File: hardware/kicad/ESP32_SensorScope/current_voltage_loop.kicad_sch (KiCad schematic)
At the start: 0 parts

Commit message: Adde LCD Part
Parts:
- added D1: D_Schottky, symbol Device:D_Schottky
- added F3: Polyfuse, symbol Device:Polyfuse
- added Q1: PMOS, symbol Simulation_SPICE:PMOS
- added Q2: NMOS, symbol Simulation_SPICE:NMOS
- added R13, R50, R51: R, symbol Device:R
- added U18, U19, U20: OPA333xxDBV, Package_TO_SOT_SMD:SOT-23-5, symbol Amplifier_Operational:OPA333xxDBV
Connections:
- new net: D1.1 (K), F3.1, Q2.1 (D)
- new net: Q2.2 (G), R13.2
- new net: Q2.3 (S), R50.2, U20.4 (-)
- new net: R13.1, U20.1
- new net: D1.2 (A), Q1.3 (S)
- new net Vref: U20.3 (+)

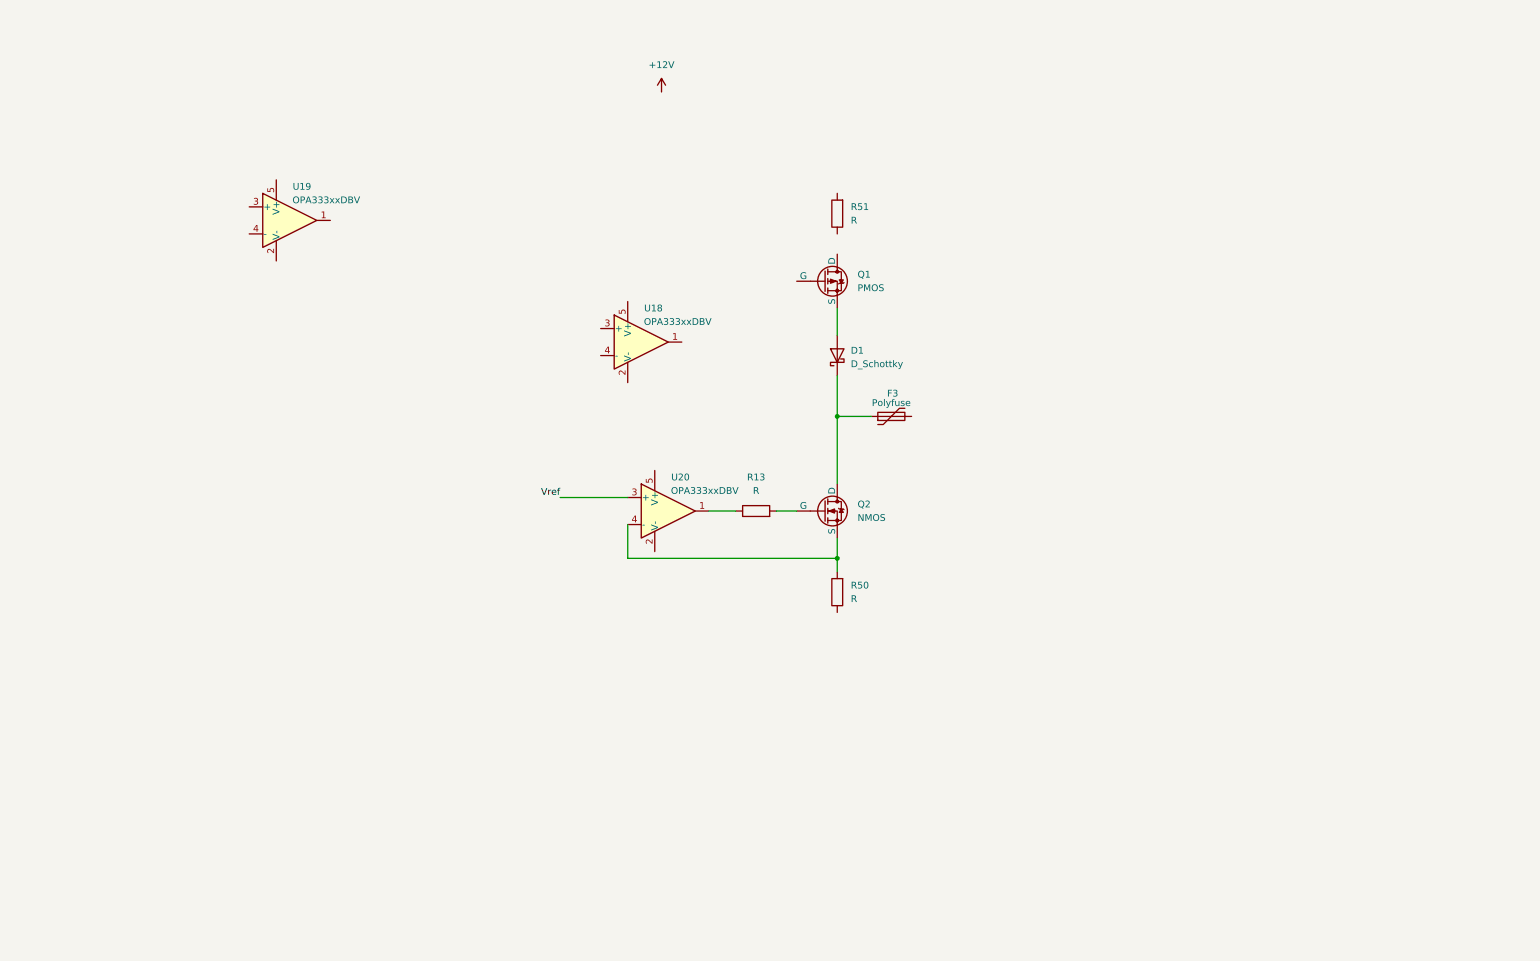
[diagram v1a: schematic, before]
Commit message: updated 4-20mA interface
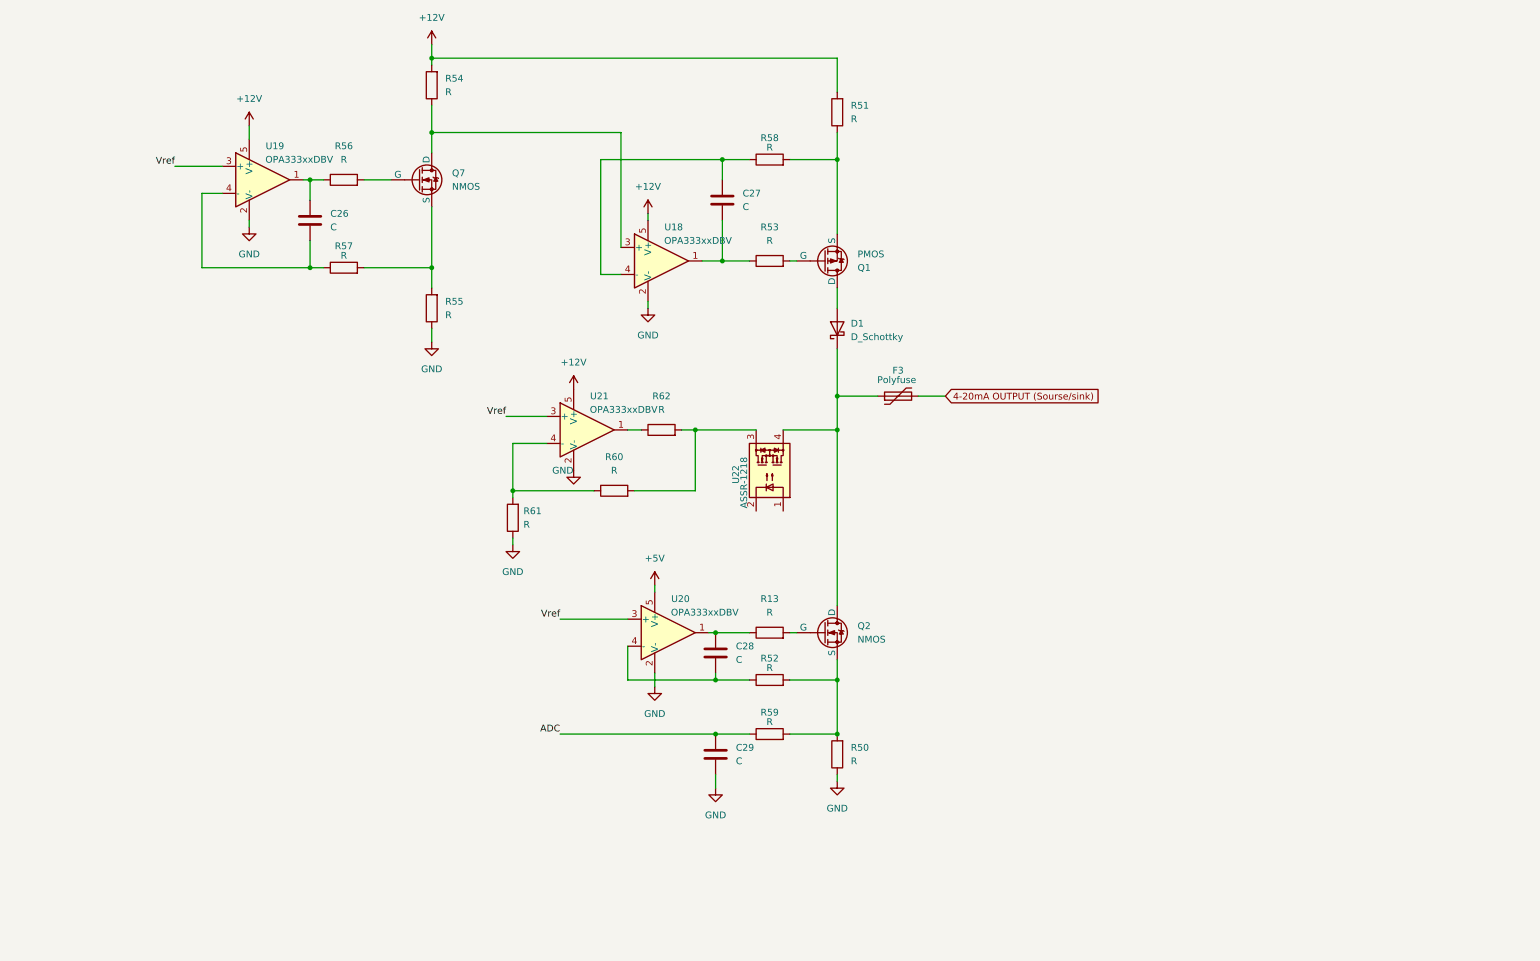
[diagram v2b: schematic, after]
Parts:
- added C26, C27, C28, C29: C, symbol Device:C
- added Q7: NMOS, symbol Simulation_SPICE:NMOS
- added R52, R53, R54, R55, R56, R57, R58, R59, R60, R61, R62: R, symbol Device:R
- added U21: OPA333xxDBV, Package_TO_SOT_SMD:SOT-23-5, symbol Amplifier_Operational:OPA333xxDBV
- added U22: ASSR-1218, Package_SO:SO-4_4.4x4.3mm_P2.54mm, symbol Relay_SolidState:ASSR-1218
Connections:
- net +12V: now also R51.2, U18.5 (V+), U19.5 (V+), R54.2, U21.5 (V+)
- net Vref: now also U19.3 (+), U21.3 (+)
- net at D1.1 (K), F3.1, Q2.1 (D): now also U22.4
- net at Q2.3 (S), R50.2: now also R52.2, R59.2; no longer U20.4 (-)
- net at R51.1: now also Q1.3 (S), R58.2
- net GND: now reaches R50.1
- net GND: now also U18.2 (V-), U19.2 (V-), U20.2 (V-), C29.2, R55.1, R61.1, U21.2 (V-)
- net at U19.1: now also C26.1, R56.1
- net at U19.4 (-): now also C26.2, R57.1
- net at R13.1, U20.1: now also C28.1
- net 4-20mA OUTPUT (Sourse/sink): now reaches F3.2
- net at D1.2 (A): now also Q1.1 (D); no longer Q1.3 (S)
- net +5V: now reaches U20.5 (V+)
- net at U18.1: now also C27.2, R53.1
- net at U18.3 (+): now also Q7.1 (D), R54.1
- net at U18.4 (-): now also C27.1, R58.1
- net at Q1.2 (G): now also R53.2
- new net: R60.2, R62.2, U22.3
- new net: C28.2, R52.1, U20.4 (-)
- new net: Q7.3 (S), R55.2, R57.2
- new net: R62.1, U21.1
- new net: R60.1, R61.2, U21.4 (-)
- new net: Q7.2 (G), R56.2
- new net ADC: C29.1, R59.1
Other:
- moved on the sheet: F3, Q1, Q2, R13, R50, R51, U18, U19, U20

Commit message: something probobly
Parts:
- added D15, D16: 15V, symbol Device:D_Zener
- added D17: D_TVS, symbol Device:D_TVS
- added D2: D_Schottky, symbol Device:D_Schottky
- added Q8: NPN, symbol Simulation_SPICE:NPN
- added Q9: PNP, symbol Simulation_SPICE:PNP
- added R63, R64, R65, R9: 10K, symbol Device:R
- added R66, R8: R, symbol Device:R
- R13, R53: value R -> 100
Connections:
- net +12V: now also D2.1 (K), R66.2
- net +5V: now also Q9.3 (E), R63.1
- net GND: now also D17.1 (A1), Q8.3 (E), R65.2, R8.1
- net at D1.1 (K), F3.1, Q2.1 (D)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: now also D16.1 (K), D17.2 (A2)
- net at Q2.2 (G), R13.2: now also D16.2 (A)
- net at Q1.3 (S), R51.1, R58.2: now also D15.1 (K)
- net at C27.2, R53.1, U18.1: now also R66.1, R9.2
- net at Q1.2 (G), R53.2: now also D15.2 (A)
- net at R62.1, U21.1: now also D2.2 (A)
- net at C28.1, R13.1, U20.1: now also R64.2, R8.2
- net ADC renamed mA_ADC
- new net: Q8.2 (B), R9.1
- new net: Q9.2 (B), R64.1
- new net Highside_Open: Q8.1 (C), R63.2
- new net Lowside_open: Q9.1 (C), R65.1
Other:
- note added: "OP-amps with shutdown OPA991 40V rail to rail, 75mA output, 125uV offset, 4.5MHz OPA990 40V rail to rail, 80mA output, 300uV offset, 1.1MHz TLV237x 16V 2000uV"
- moved on the sheet: C26, C27, C28, C29, F3, Q1, Q2, Q7, R13, R50, R51, R52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

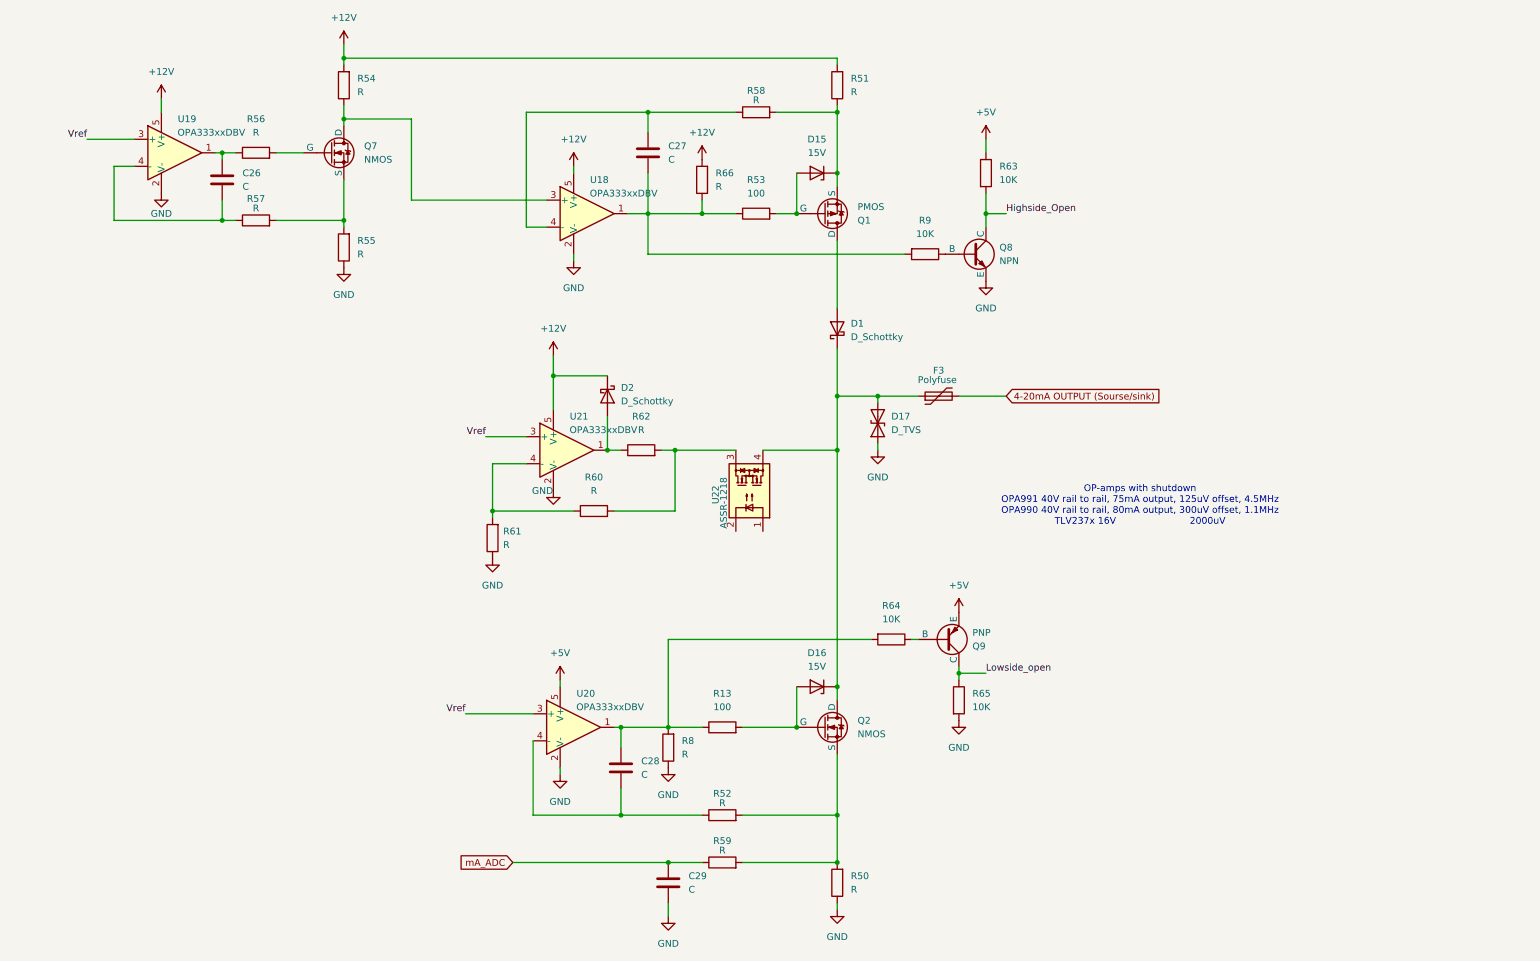
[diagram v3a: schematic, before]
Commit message: som updates on the schematics
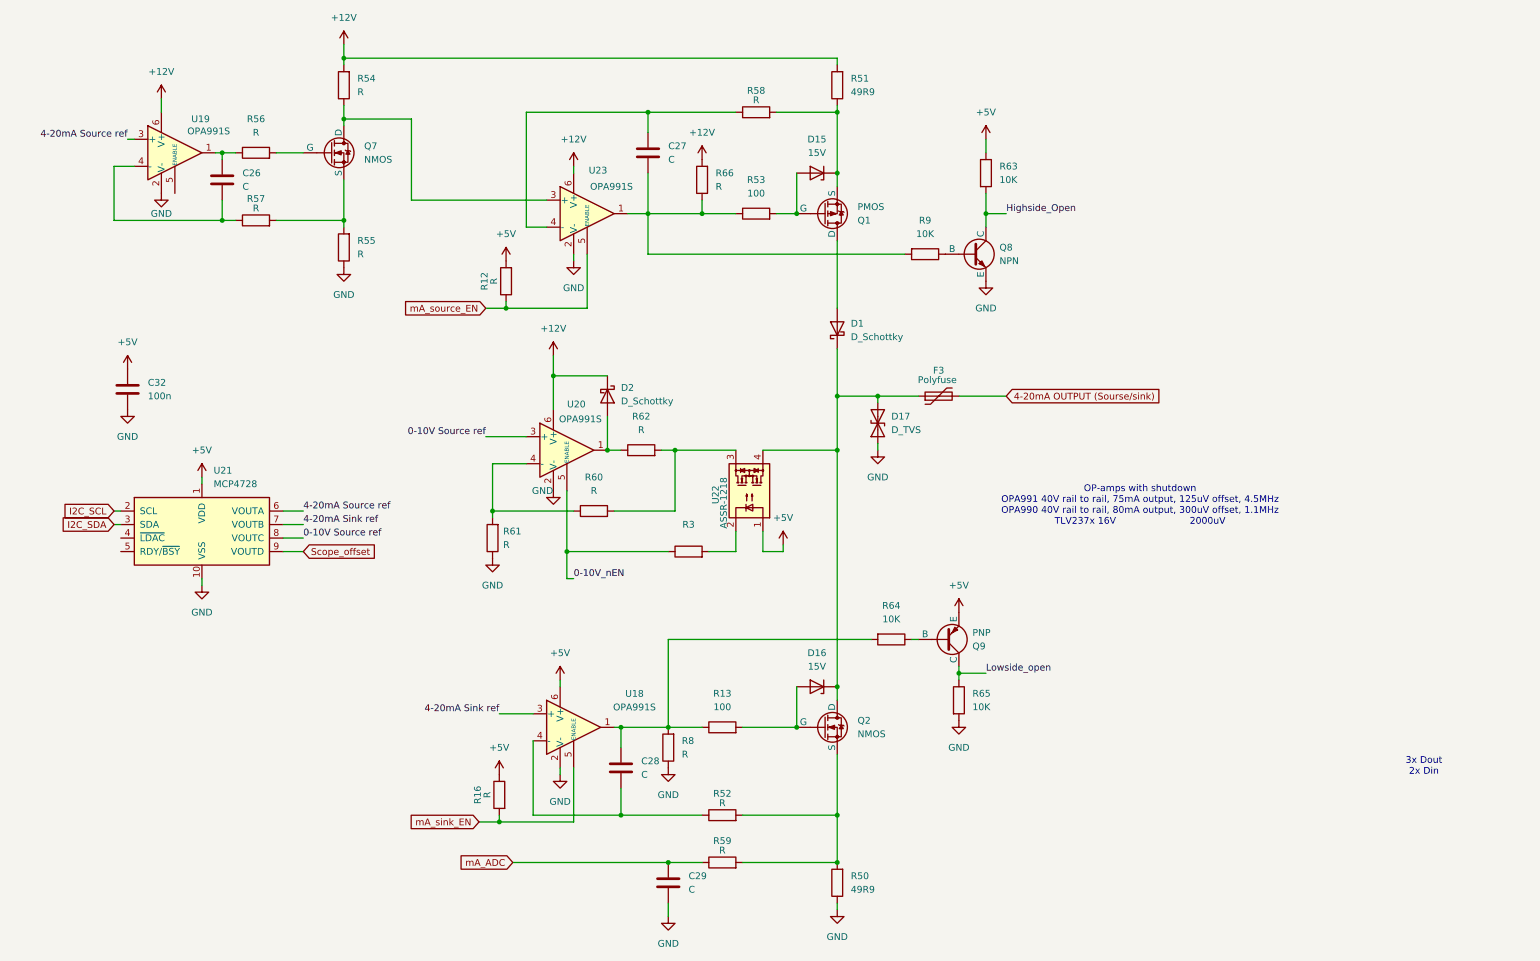
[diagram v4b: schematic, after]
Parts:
- removed U18, U19, U20, U21: OPA333xxDBV, Package_TO_SOT_SMD:SOT-23-5, symbol Amplifier_Operational:OPA333xxDBV
- added C32: 100n, symbol Device:C
- added R12, R16: R, symbol Device:R
- added R3: ~, symbol Device:R
- added U18, U19, U20, U23: OPA991S, Package_TO_SOT_SMD:SOT-23-6, symbol My_library:OPA991S
- added U21: MCP4728, Package_SO:MSOP-10_3x3mm_P0.5mm, symbol Analog_DAC:MCP4728
- R50, R51: value R -> 49R9; footprint (none) -> Resistor_SMD:R_1206_3216Metric
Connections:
- net +12V: now also U19.6 (V+), U20.6 (V+), U23.6 (V+)
- net +5V: now also U22.1, C32.1, R12.2, R16.1, U18.6 (V+), U21.1 (VDD)
- net GND: now also C32.2, U18.2 (V-), U19.2 (V-), U20.2 (V-), U21.10 (VSS), U23.2 (V-)
- net at C27.2, R53.1, R66.1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: now also U23.1
- net at U22.2: now also R3.2
- net at C28.2, R52.1: now also U18.4 (-)
- net at C26.2, R57.1: now also U19.4 (-)
- net at C27.1, R58.1: now also U23.4 (-)
- net at D2.2 (A), R62.1: now also U20.1
- net at C28.1, R13.1, R64.2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: now also U18.1
- net at C26.1, R56.1: now also U19.1
- net at R60.1, R61.2: now also U20.4 (-)
- net at Q7.1 (D), R54.1: now also U23.3 (+)
- new net 0-10V Source ref: U20.3 (+), U21.8 (VOUTC)
- new net 0-10V_nEN: R3.1, U20.5 (ENABLE)
- new net 4-20mA Sink ref: U18.3 (+), U21.7 (VOUTB)
- new net 4-20mA Source ref: U19.3 (+), U21.6 (VOUTA)
- new net I2C_SCL: U21.2 (SCL)
- new net I2C_SDA: U21.3 (SDA)
- new net Scope_offset: U21.9 (VOUTD)
- new net mA_sink_EN: R16.2, U18.5 (ENABLE)
- new net mA_source_EN: R12.1, U23.5 (ENABLE)
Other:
- note added: "3x Dout 2x Din"

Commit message: updatet schematic
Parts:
- removed C32: 100n, symbol Device:C
- removed U21: MCP4728, Package_SO:MSOP-10_3x3mm_P0.5mm, symbol Analog_DAC:MCP4728
- added D10: D_Schottky, symbol Device:D_Schottky
- R64, R9: value 10K -> 100K
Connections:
- net mA_source_EN: now also U19.5 (ENABLE)
- net at D1.1 (K), D17.2 (A2), F3.1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: now also D10.2 (A); no longer D16.1 (K), Q2.1 (D)
- net 0-10V Source ref renamed 0-10V_source_ref
- net 4-20mA Sink ref renamed 4-20mA_sink_ref
- net 4-20mA Source ref renamed 4-20mA_source_ref
- net Highside_Open renamed mA_source_open
- net Lowside_open renamed mA_sink_open
- new net: D10.1 (K), D16.1 (K), Q2.1 (D)
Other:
- moved on the sheet: C26, C27, C28, C29, D1, D15, D16, D17, D2, F3, Q1, Q2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
